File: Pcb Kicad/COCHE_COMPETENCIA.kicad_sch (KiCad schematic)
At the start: 26 parts, among them J1 BAT, J2 SWITCH, J4 M1, J5 M2, J6 SENSORES, SW1 SW_Push, SW2 SW_Push, U1 L7805, U2 ESP32-DEVKIT-V1, U3 DRV8833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

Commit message: V1.1 - Correccion de bocina y programas de motores.
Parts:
- added D2: 1N4148, Diode_THT:D_DO-35_SOD27_P7.62mm_Horizontal, symbol Diode:1N4148
- added Q1: 2N3904, Package_TO_SOT_THT:TO-92_Inline_Wide, symbol Transistor_BJT:2N3904
- D1: footprint LED_SMD:LED_1206_3216Metric_Pad1.42x1.75mm_HandSolder -> LED_THT:LED_D5.0mm
- R7: value 0 -> 1k
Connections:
- net GND: now also Q1.1 (E); no longer BZ1.2 (-)
- net VCC: now also BZ1.1 (+), D2.1 (K)
- net at R7.2: now also Q1.2 (B); no longer BZ1.1 (+)
- new net: BZ1.2 (-), D2.2 (A), Q1.3 (C)
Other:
- moved on the sheet: BZ1, C1, C2, H1, H2, H3, H4, R7, U1

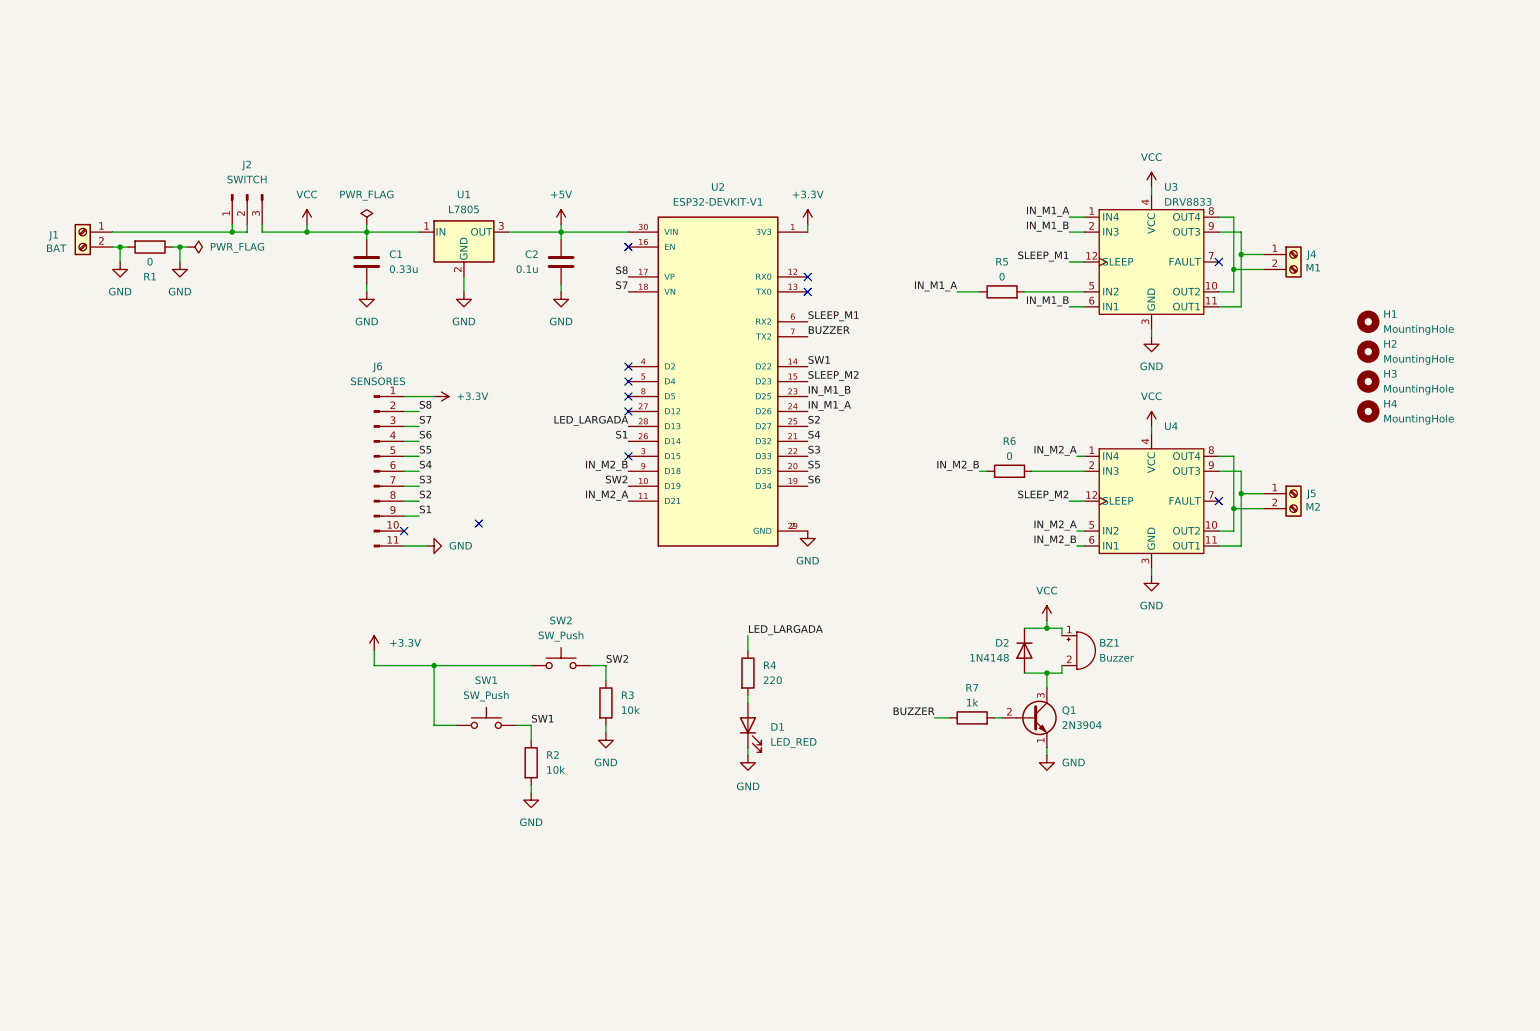
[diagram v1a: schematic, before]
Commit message: V1.2 - Mejoras de PCB: alimentacion, bocina y borneras.
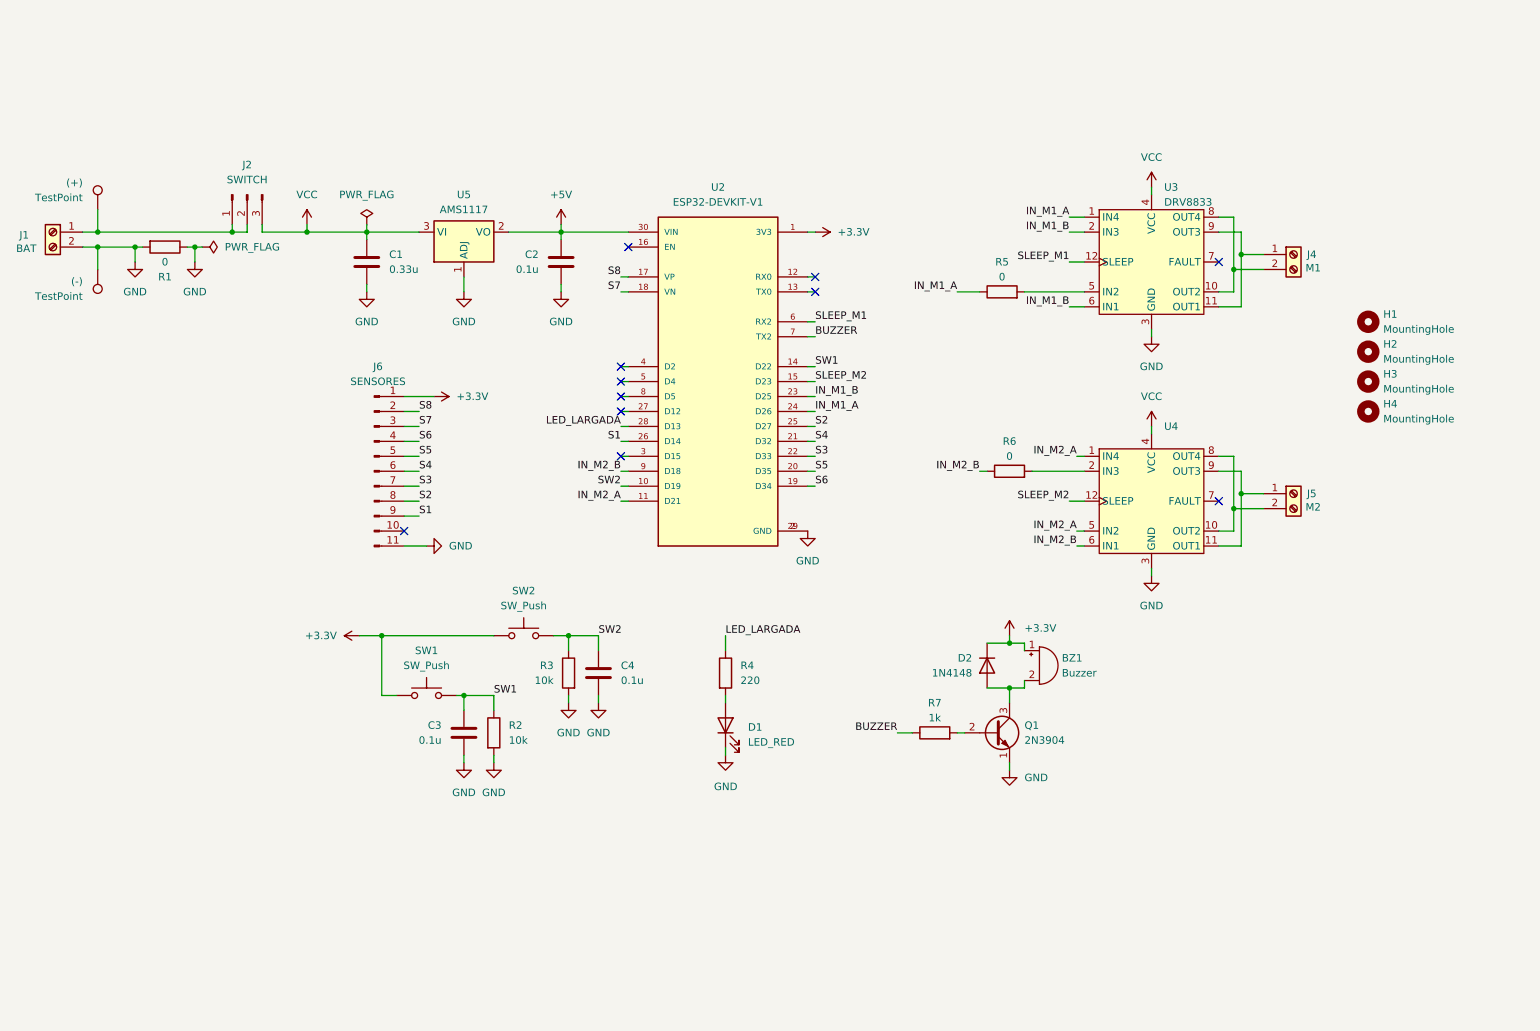
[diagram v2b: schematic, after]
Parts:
- removed U1: L7805, Package_TO_SOT_SMD:TO-252-3_TabPin2, symbol Regulator_Linear:L7805
- added (+), (-): TestPoint, Connector_PinHeader_2.54mm:PinHeader_1x01_P2.54mm_Vertical, symbol Connector:TestPoint
- added C3, C4: 0.1u, Capacitor_SMD:C_1206_3216Metric_Pad1.33x1.80mm_HandSolder, symbol Device:C
- added U5: AMS1117, Package_TO_SOT_SMD:SOT-223-3_TabPin2, symbol Regulator_Linear:AMS1117
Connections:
- net +3.3V: now also BZ1.1 (+), D2.1 (K)
- net +5V: now also U5.2 (VO)
- net GND: now also (-).1, C3.2, C4.2, U5.1 (ADJ)
- net SW1: now also C3.1
- net SW2: now also C4.1
- net VCC: now also U5.3 (VI); no longer BZ1.1 (+), D2.1 (K)
- net at J1.1 (Pin_1), J2.1 (Pin_1), J2.2 (Pin_2): now also (+).1
- no-connect marks 12 -> 11
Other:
- moved on the sheet: BZ1, D1, D2, J1, Q1, R1, R2, R3, R4, R7, SW1, SW2

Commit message: V1.3 - Diodo de proteccion + Mejor ubicacion de Sw's
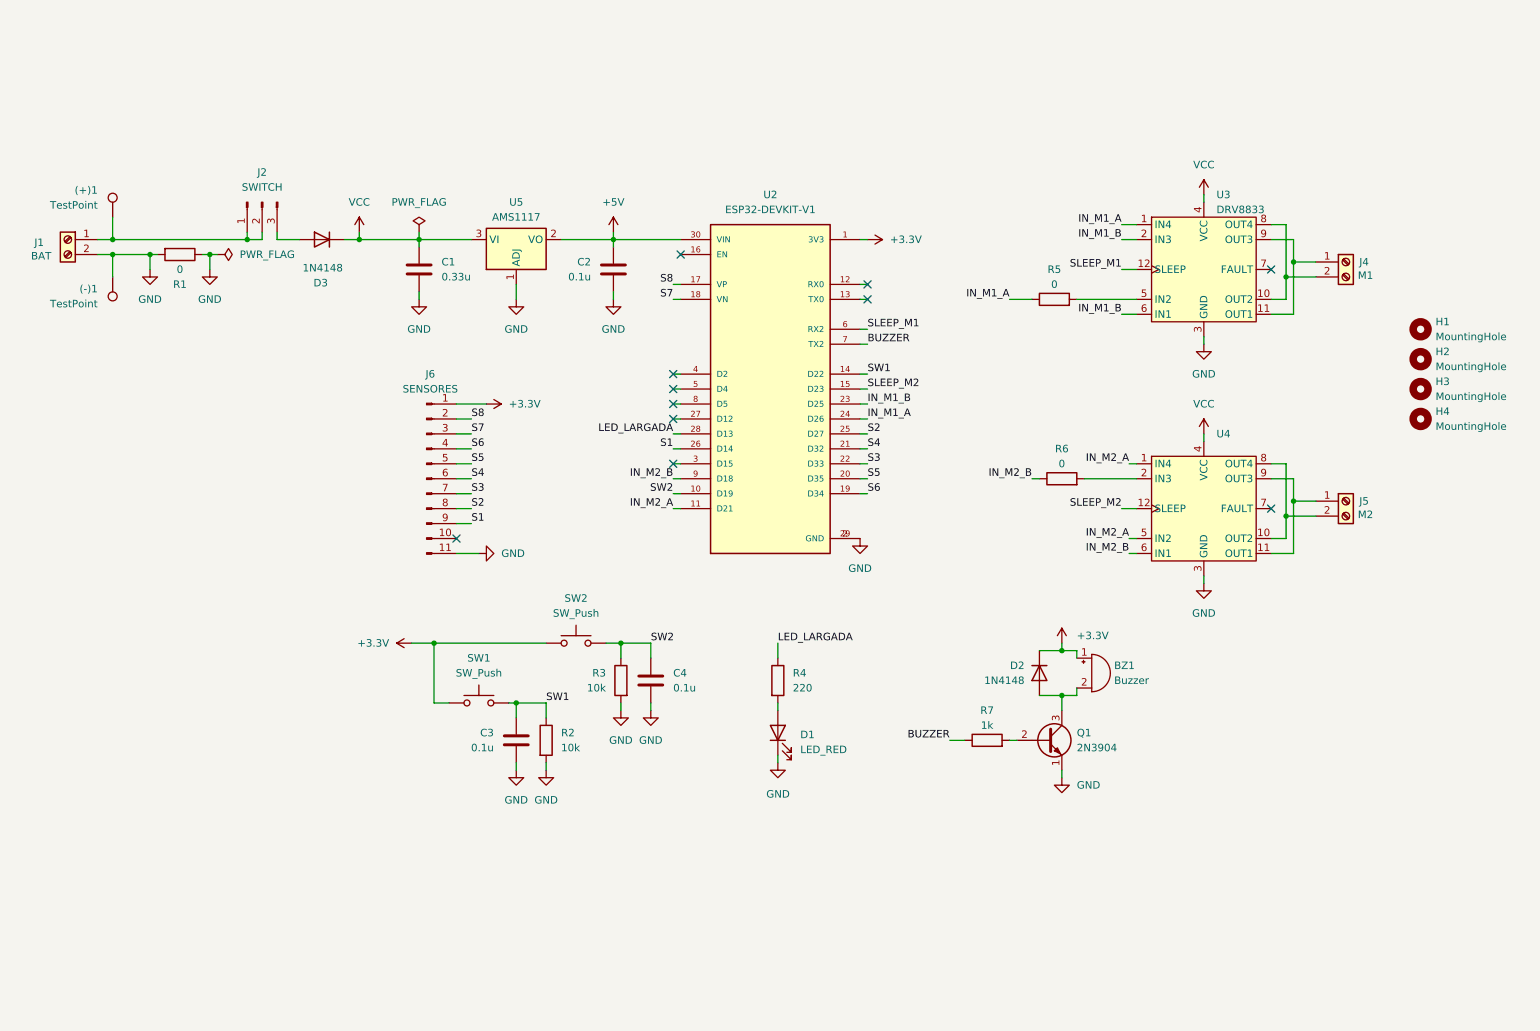
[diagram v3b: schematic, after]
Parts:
- added D3: 1N4148, Diode_THT:D_DO-35_SOD27_P7.62mm_Horizontal, symbol Diode:1N4148
- renumbered (+) to (+)1, (-) to (-)1
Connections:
- net VCC: now also D3.1 (K); no longer J2.3 (Pin_3)
- new net: D3.2 (A), J2.3 (Pin_3)
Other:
- moved on the sheet: (+)1, (-)1, BZ1, C1, C2, C3, C4, D1, D2, H1, H2, H3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

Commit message: V1.3 - Agregado de Prot. Tension inversa & pull downs y acomodado de componentes.
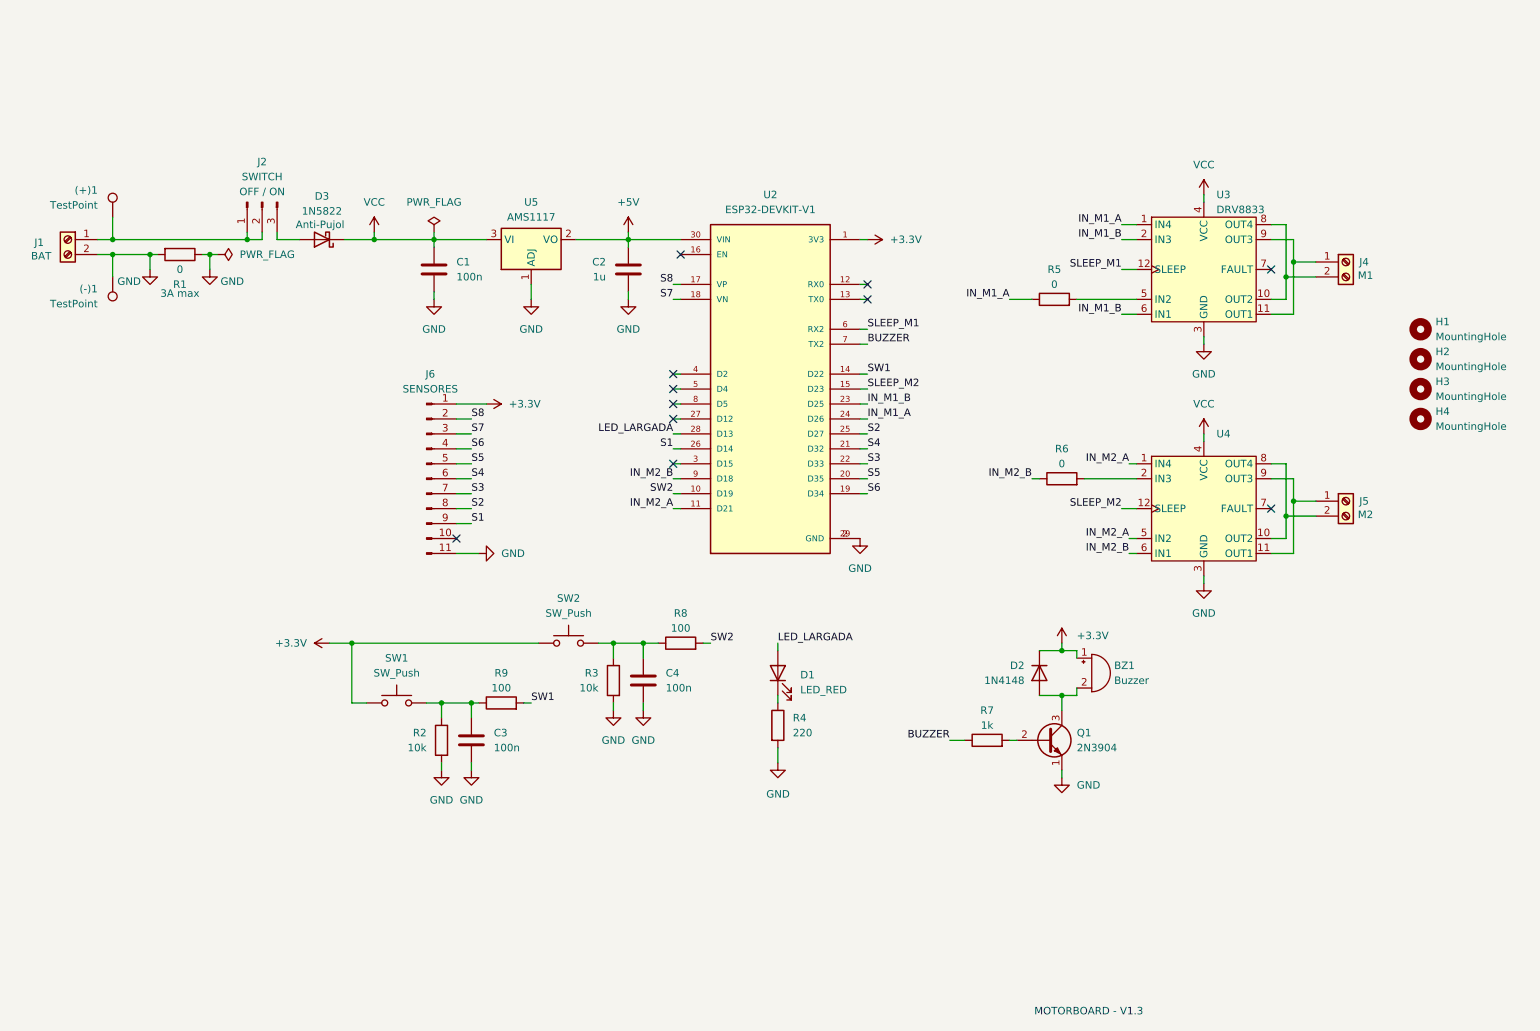
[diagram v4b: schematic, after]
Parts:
- removed D3: 1N4148, Diode_THT:D_DO-35_SOD27_P7.62mm_Horizontal, symbol Diode:1N4148
- added D3: 1N5822, Diode_THT:D_DO-201AD_P12.70mm_Horizontal, symbol Diode:1N5822
- added R8, R9: 100, Resistor_SMD:R_1206_3216Metric_Pad1.30x1.75mm_HandSolder, symbol Device:R
- C1: value 0.33u -> 100n
- C2: value 0.1u -> 1u
- C3, C4: value 0.1u -> 100n
- J2: text (none) -> OFF / ON
- R1: text (none) -> 3A max
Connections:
- net GND: now also R4.2; no longer D1.1 (K)
- net LED_LARGADA: now also D1.2 (A); no longer R4.1
- net SW1: now also R9.2; no longer C3.1, R2.1, SW1.2
- net SW2: now also R8.2; no longer C4.1, R3.1, SW2.2
- net VCC: now also D3.1 (K)
- net at J2.3 (Pin_3): now also D3.2 (A)
- new net: C3.1, R2.1, R9.1, SW1.2
- new net: D1.1 (K), R4.1
- new net: C4.1, R3.1, R8.1, SW2.2
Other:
- note added: "MOTORBOARD - V1.3"
- moved on the sheet: C1, C2, C3, C4, D1, R2, R3, R4, SW1, SW2, U5

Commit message: V1.4 - Mejores pistas & Modulo de Interrupciones
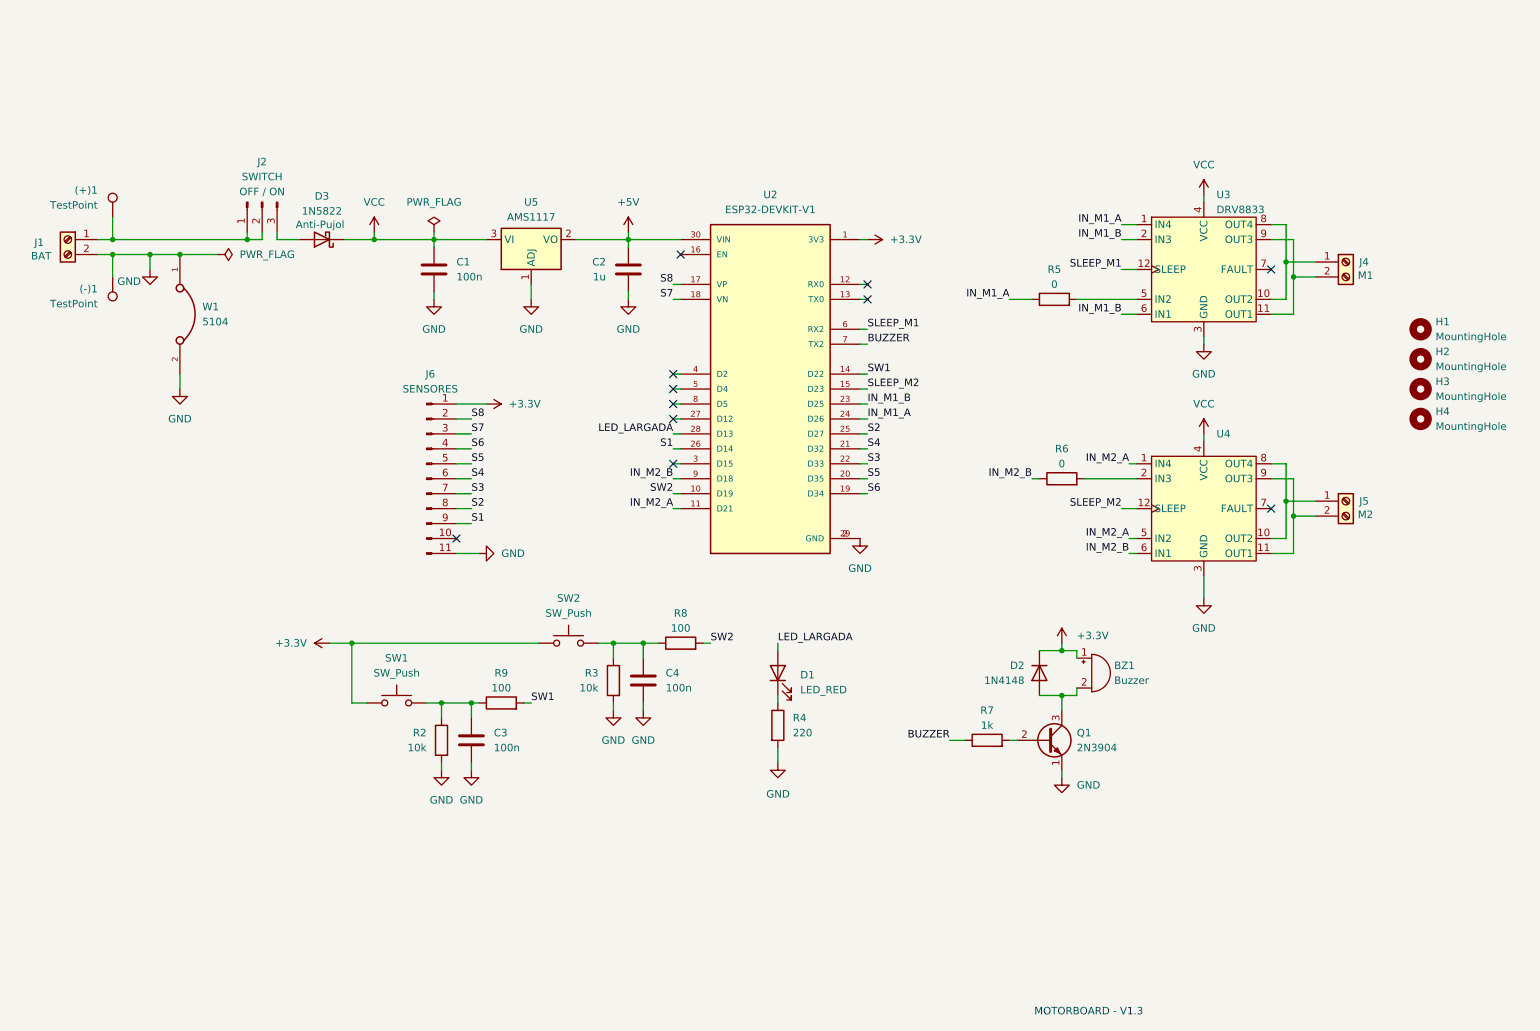
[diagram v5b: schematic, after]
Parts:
- removed R1: 0, Resistor_SMD:R_1206_3216Metric_Pad1.30x1.75mm_HandSolder, symbol Device:R
- added W1: 5104, JUMPLER 5104:KEYSTONE_5104, symbol 5104:5104
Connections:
- net GND: now also W1.1, W1.2
- net at U3.11 (OUT1), U3.9 (OUT3): now also J4.2 (Pin_2); no longer J4.1 (Pin_1)
- net at U3.10 (OUT2), U3.8 (OUT4): now also J4.1 (Pin_1); no longer J4.2 (Pin_2)
- net at U4.10 (OUT2), U4.8 (OUT4): now also J5.1 (Pin_1); no longer J5.2 (Pin_2)
- net at U4.11 (OUT1), U4.9 (OUT3): now also J5.2 (Pin_2); no longer J5.1 (Pin_1)

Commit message: V1.4 - Programa seguidor Modular
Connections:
- net LED_BUILDIN: now reaches U2.4 (D2)
- no-connect marks 11 -> 10
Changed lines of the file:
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@@
 	)
 	(no_connect
-		(at 128.27 81.28)
-	)
-	(no_connect
 		(at 161.29 66.04)
 	)
@@
 			"AAAAAAAAAAAAAAAAAAAAAAAAAAAAAAAAAAAAAAAAAAAAAAAAAAAAAAAAAAAAAAAAAAAAAAAAAAAA"
 			"AAAAAAAAAAAAAAAAAAAAAAAAAAAAAAAAAAAAAAAAAAAAAAAAAAAAAAAAAAAAAAAAAAAAAAAAAAAA"
-			"AAAAAAAAAAAAAAAAAAAAAAAAAAAAAAAAAAAAAAAAAAAAAA=="
+			"AAAAAAAAAAAAAAAAAAAAAAAAAAAAAAAAAAAAAAAAAAAAAA0KCQkJCSh4eXogMSAxIDEpDQoJCQkp"
+			"DQoJCQkocm90YXRlDQoJCQkJKHh5eiAwIDAgMCkNCgkJCSkNCgkJKQ0KCSkNCgkoZm9vdHByaW50"
+			"ICJNb3VudGluZ0hvbGU6TW91bnRpbmdIb2xlXzNtbSINCgkJKGxheWVyICJGLkN1IikNCgkJKHV1"
+			"aWQgImY5MzNmZjEyLTgxNzItNDhlNS1iZGU3LTI4MDFjZWJkMTJjMiIpDQoJCShhdCAxMDAuODM4"
+			"IDI4LjgyOSAxODApDQoJCShkZXNjciAiTW91bnRpbmcgSG9sZSAzbW0sIG5vIGFubnVsYXIiKQ0K"
+			"CQkodGFncyAibW91bnRpbmcgaG9sZSAzbW0gbm8gYW5udWxhciIpDQoJCShwcm9wZXJ0eSAiUmVm"
+			"ZXJlbmNlIiAiSDEiDQoJCQkoYXQgMCAtNCAwKQ0KCQkJKGxheWVyICJGLlNpbGtTIikNCgkJCSho"
+			"aWRlIHllcykNCgkJCSh1dWlkICJkODMxM2E0Yy1lZjg1LTQzODktOWI1NC0wMjRmYmJiNzE1ZjAi"
+			"KQ0KCQkJKGVmZmVjdHMNCgkJCQkoZm9udA0KCQkJCQkoc2l6ZSAxIDEpDQoJCQkJCSh0aGlja25l"
+			"c3MgMC4xNSkNCgkJCQkpDQoJCQkpDQoJCSkNCgkJKHByb3BlcnR5ICJWYWx1ZSIgIk1vdW50aW5n"
+			"SG9sZSINCgkJCShhdCAwIC04LjEyOCAyNzApDQoJCQkobGF5ZXIgIkYuRmFiIikNCgkJCSh1dWlk"
+			"ICI4OTQzY2FkYS0zNDExLTRkMjAtYWM5Yy0yYmIyMDE3ODFhOWMiKQ0KCQkJKGVmZmVjdHMNCgkJ"
+			"CQkoZm9udA0KCQkJCQkoc2l6ZSAxIDEpDQoJCQkJCSh0aGlja25lc3MgMC4xNSkNCgkJCQkpDQoJ"
+			"CQkpDQoJCSkNCgkJKHByb3BlcnR5ICJEYXRhc2hlZXQiICIiDQoJCQkoYXQgMCAwIDE4MCkNCgkJ"
+			"CSh1bmxvY2tlZCB5ZXMpDQoJCQkobGF5ZXIgIkYuRmFiIikNCgkJCShoaWRlIHllcykNCgkJCSh1"
+			"dWlkICJlNjFmNWQxNy1hOTE3LTRkOWYtYTBiZS0wZjVmYWNlODVlNWEiKQ0KCQkJKGVmZmVjdHMN"
+			"CgkJCQkoZm9udA0KCQkJCQkoc2l6ZSAxLjI3IDEuMjcpDQoJCQkJCSh0aGlja25lc3MgMC4xNSkN"
+			"CgkJCQkpDQoJCQkpDQoJCSkNCgkJKHByb3BlcnR5ICJEZXNjcmlwdGlvbiIgIk1vdW50aW5nIEhv"
+			"bGUgd2l0aG91dCBjb25uZWN0aW9uIg0KCQkJKGF0IDAgMA=="
 		)
 	)
@@
 		(effects
 			(font
+				(size 1.27 1.27)
+			)
+			(justify right bottom)
+		)
+	)
+	(label "LED_BUILDIN"
+		(at 128.27 81.28 180)
+		(effects
+			(font
